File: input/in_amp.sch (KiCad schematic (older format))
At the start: 18 parts, among them J101 Conn_02x02_Odd_Even, U105 LT1028, U106 LT1028, U107 LT1028

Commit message: Changes mostly related to avoiding excess power consumption.  This is mainly by limiting the signal swing to 0..5V and using asymmetric supplies of -4V and +8V.  (Perhaps we can reduce these to 3/7 V.)  Also, I got rid of two stages in the input signal path.
power_budget.xlsx
power.sch
reference_buffer.sch:
Changes related to the new supply voltages, and start on the power supply section.

input_channel.sch
in_amp.sch
antialias_driver.sch:
Reworked the input signal chain to keep a full differential path, rolling the antialias filter
into the ADC driver.  Also, related to change to lower asymmetrical supply voltages, there is
no 20V PP anywhere (the this was for benefit of the antialias filter noise, but that stage is gone).  Also, added zener clamp on VREF in driver.

in_filter.sch: added missing DC bias resistors.
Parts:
- removed C133, C134, C135, C136: 1uF, Capacitor_SMD:C_0603_1608Metric, symbol Device:C_Small
- removed RN103: 1K, Resistor_SMD:R_Array_Convex_4x1206, symbol Device:R_Pack04
- removed U105, U106, U107: LT1028, symbol ilemt_input:opamp_single
- added U101: AD8599, Package_SO:SO-8_5.3x6.2mm_P1.27mm, symbol ilemt_input:OPAMP_DUAL
- R126: value 49.9 -> 100; Notes (none) -> 0.1%
- R127: value 143 -> 243
- R128: value 499 -> 1K; footprint Resistor_SMD:R_1206_3216Metric -> Resistor_SMD:R_0603_1608Metric; Description RES 499 OHM 0.1% 2/5W 1206 -> (none); Digikey 541-3877-1-ND -> (none)
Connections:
- net labels added: +out, -out, V+, V-
- net labels removed: +15V, -15V, out, out_ref
- wire segments 79 -> 47
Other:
- note added: "Both jumpers: gain 16\nJumper 1-2: gain 12\nJumper 3-4: gain 6\nNo jumpers: gain 2\n"
- note added: "C129, C130 give a pole at 30 kHz which is part of the 3rd order\nantialias filter. They also swamp stray capacitance at the\ninverting input due to gain switching network."
- note added: "This is a differential amplifier, like the first part of a 3 opamp style \ninstrumentation amp, but we output to the fully-differential\ndriver/antialias filter in the antialias_driver sheet."
- note removed: "Both jumpers: gain 30\nJumper 1-2: gain 21\nJumper 3-4: gain 10\nNo jumpers: gain 3\nNote that ADC driver has gain 1/2, \nso overall gain is half this\n"
- note removed: "C195, C1230 mainly there to swamp excess capacitance at the \ninverting input due to gain switching network, but also give\nsome band limiting, 144 kHz. The antialias filter gives plenty\nof rejection, so we are not risking compromising CMR by\ntaking a strong cut here (though to first order, mismatch should\nnot matter)."

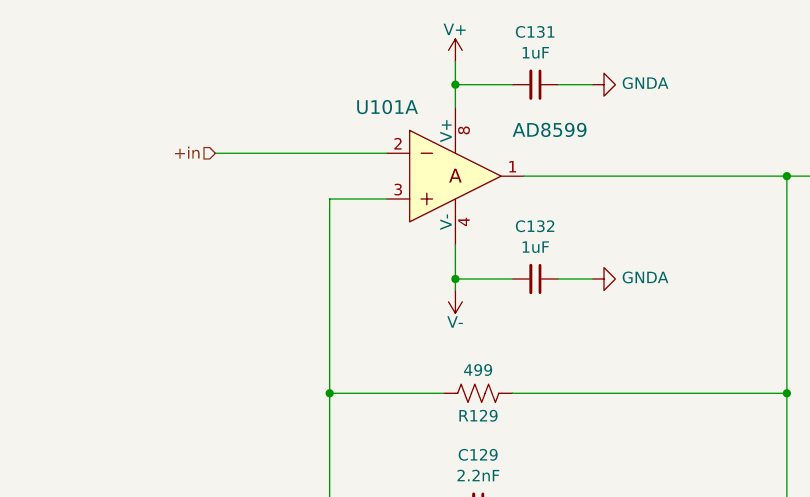
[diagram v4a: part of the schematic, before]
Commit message: Mostly work on power, regulators and distribution.  Also more BOM cleanup.
All of the bypass capacitors are now spec'd and in the DigiKey BOM. TVS zeners are now
spec'd.  Folded together some resistor values and got rid of some 1206 parts that no longer
need that much power rating at the lower supplies.

A affecting all of the input channel sheets is that we now distribute filtered V+, V- and VREF
via sheet ports.  The V+, V- filter is on input_channel.sch and the VREF filter is still in
adc.sch, but is distributed out to the other sheets that need it.

bist_buffer.sch: added buffer for built-in self-test

board_connector.sch: put the input filter for the analog supplies here.

power.sch: added regulators for the supplies.

reference_buffer.sch:
changed components to match those chosen for the V+, V- regulators and added
current steering diodes to bootstrap the reference buffer supply.  This is
necessary because the analog supplies are now derived from VREF.

*.wxsch:
Updates to spice models related to work on supplies.
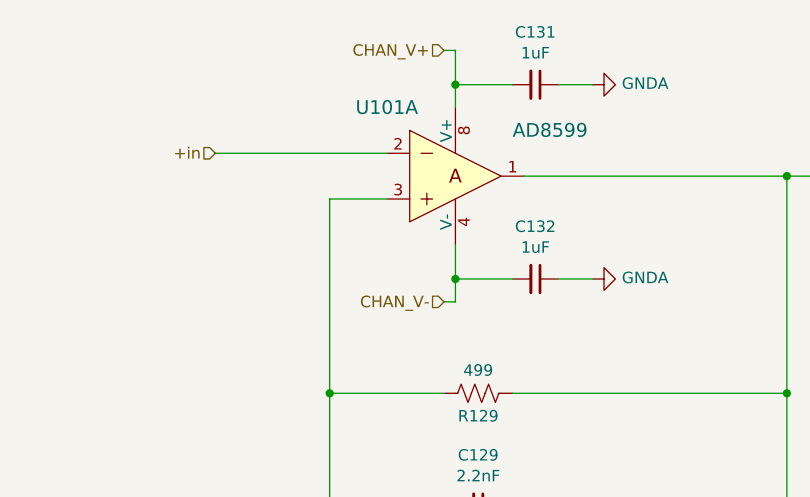
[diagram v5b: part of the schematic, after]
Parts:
- C131, C132: footprint Capacitor_SMD:C_0603_1608Metric -> Capacitor_SMD:C_0805_2012Metric; Description (none) -> CAP CER 1UF 16V X7R 0805; Digikey (none) -> 1276-6471-1-ND; MPN (none) -> CL21B105KOFNNNG
- R128: Notes (none) -> 0.1%
- R129, R130: footprint Resistor_SMD:R_1206_3216Metric -> Resistor_SMD:R_0805_2012Metric; Description RES 499 OHM 0.1% 2/5W 1206 -> RES SMD 499 OHM 0.1% 1/4W 0805; Digikey 541-3877-1-ND -> A110514CT-ND; Notes (none) -> 0.1%
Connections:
- net V+ renamed CHAN_V+
- net V- renamed CHAN_V-
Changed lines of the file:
@@
 EESchema Schematic File Version 4
 LIBS:input_board-cache
-LIBS:input_channel-cache
-LIBS:reference_buffer-cache
 EELAYER 29 0
 EELAYER END
 $Descr A4 11693 8268
 encoding utf-8
-Sheet 6 11
+Sheet 6 12
 Title ""
 Date ""
@@
 Comment4 ""
 $EndDescr
-Wire Wire Line
-	4000 900  4000 1000
 $Comp
 L Device:C_Small C131
@@
 F 0 "C131" V 4121 1000 50  0000 C CNN
 F 1 "1uF" V 4212 1000 50  0000 C CNN
-F 2 "Capacitor_SMD:C_0603_1608Metric" H 4350 1000 50  0001 C CNN
-F 3 "~" H 4350 1000 50  0001 C CNN
+F 2 "Capacitor_SMD:C_0805_2012Metric" H 4350 1000 50  0001 C CNN
+F 3 "https://media.digikey.com/pdf/Data%20Sheets/Samsung%20PDFs/CL_Series_MLCC_ds.pdf" H 4350 1000 50  0001 C CNN
+F 4 "CAP CER 1UF 16V X7R 0805 " H 4350 1000 50  0001 C CNN "Description"
+F 5 "1276-6471-1-ND" H 4350 1000 50  0001 C CNN "Digikey"
+F 6 "CL21B105KOFNNNG" H 4350 1000 50  0001 C CNN "MPN"
 	1    4350 1000
 	0    1    1    0
@@
 F 0 "C132" V 4121 1850 50  0000 C CNN
 F 1 "1uF" V 4212 1850 50  0000 C CNN
-F 2 "Capacitor_SMD:C_0603_1608Metric" H 4350 1850 50  0001 C CNN
-F 3 "~" H 4350 1850 50  0001 C CNN
+F 2 "Capacitor_SMD:C_0805_2012Metric" H 4350 1850 50  0001 C CNN
+F 3 "https://media.digikey.com/pdf/Data%20Sheets/Samsung%20PDFs/CL_Series_MLCC_ds.pdf" H 4350 1850 50  0001 C CNN
+F 4 "CAP CER 1UF 16V X7R 0805 " H 4350 1850 50  0001 C CNN "Description"
+F 5 "1276-6471-1-ND" H 4350 1850 50  0001 C CNN "Digikey"
+F 6 "CL21B105KOFNNNG" H 4350 1850 50  0001 C CNN "MPN"
 	1    4350 1850
 	0    1    1    0
@@
 Wire Wire Line
 	4450 1850 4600 1850
-Wire Wire Line
-	4000 1900 4000 1850
 Connection ~ 4000 1850
 Wire Wire Line
@@
 F 0 "R129" V 4200 2350 50  0000 C CNN
 F 1 "499" V 4000 2350 50  0000 C CNN
-F 2 "Resistor_SMD:R_1206_3216Metric" V 4140 2340 50  0001 C CNN
+F 2 "Resistor_SMD:R_0805_2012Metric" V 4140 2340 50  0001 C CNN
 F 3 "http://www.vishay.com/docs/28758/tnpw_e3.pdf" H 4100 2350 50  0001 C CNN
-F 4 "RES 499 OHM 0.1% 2/5W 1206" H 4100 2350 50  0001 C CNN "Description"
-F 5 "541-3877-1-ND" H 4100 2350 50  0001 C CNN "Digikey"
+F 4 "RES SMD 499 OHM 0.1% 1/4W 0805" H 4100 2350 50  0001 C CNN "Description"
+F 5 "A110514CT-ND" H 4100 2350 50  0001 C CNN "Digikey"
+F 6 "0.1%" H 4100 2350 50  0001 C CNN "Notes"
 	1    4100 2350
 	0    1    1    0
@@
 F 0 "R130" V 4200 5250 50  0000 C CNN
 F 1 "499" V 4000 5250 50  0000 C CNN
-F 2 "Resistor_SMD:R_1206_3216Metric" V 4140 5240 50  0001 C CNN
+F 2 "Resistor_SMD:R_0805_2012Metric" V 4140 5240 50  0001 C CNN
 F 3 "http://www.vishay.com/docs/28758/tnpw_e3.pdf" H 4100 5250 50  0001 C CNN
-F 4 "RES 499 OHM 0.1% 2/5W 1206" H 4100 5250 50  0001 C CNN "Description"
-F 5 "541-3877-1-ND" H 4100 5250 50  0001 C CNN "Digikey"
+F 4 "RES SMD 499 OHM 0.1% 1/4W 0805" H 4100 5250 50  0001 C CNN "Description"
+F 5 "A110514CT-ND" H 4100 5250 50  0001 C CNN "Digikey"
+F 6 "0.1%" H 4100 5250 50  0001 C CNN "Notes"
 	1    4100 5250
 	0    1    1    0
@@
 F 2 "Resistor_SMD:R_0603_1608Metric" V 3940 4040 50  0001 C CNN
 F 3 "http://www.vishay.com/docs/28758/tnpw_e3.pdf" H 3900 4050 50  0001 C CNN
+F 4 "0.1%" H 3900 4050 50  0001 C CNN "Notes"
 	1    3900 4050
 	1    0    0    -1
@@
 This is a differential amplifier, like the first part of a 3 opamp style \ninstrumentation amp, but we output to the fully-differential\ndriver/antialias filter in the antialias_driver sheet.
 $Comp
-L ilemt_input:V+ #PWR0132
-U 1 1 5E4F57E2
-P 4000 900
-F 0 "#PWR0132" H 4000 750 50  0001 C CNN
-F 1 "V+" H 4000 1040 50  0000 C CNN
-F 2 "" H 4000 900 50  0001 C CNN
-F 3 "" H 4000 900 50  0001 C CNN
-	1    4000 900
-	1    0    0    -1
-$EndComp
-$Comp
-L ilemt_input:V- #PWR0139
-U 1 1 5E4F5C06
-P 4000 2000
-F 0 "#PWR0139" H 4000 1850 50  0001 C CNN
-F 1 "V-" H 4000 1960 50  0000 C CNN
-F 2 "" H 4000 2100 50  0001 C CNN
-F 3 "" H 4000 2100 50  0001 C CNN
-	1    4000 2000
-	1    0    0    -1
-$EndComp
-$Comp
 L ilemt_input:OPAMP_DUAL U101
 U 1 1 5E501ACE
@@
 	5450 5250 5450 6050
 Connection ~ 5450 5250
+Text HLabel 3950 850  0    50   Input ~ 0
+CHAN_V+
+Text HLabel 3950 1950 0    50   Input ~ 0
+CHAN_V-
+Wire Wire Line
+	3950 850  4000 850
+Wire Wire Line
+	4000 850  4000 1000
+Wire Wire Line
+	3950 1950 4000 1950
+Wire Wire Line
+	4000 1850 4000 1950
 $EndSCHEMATC

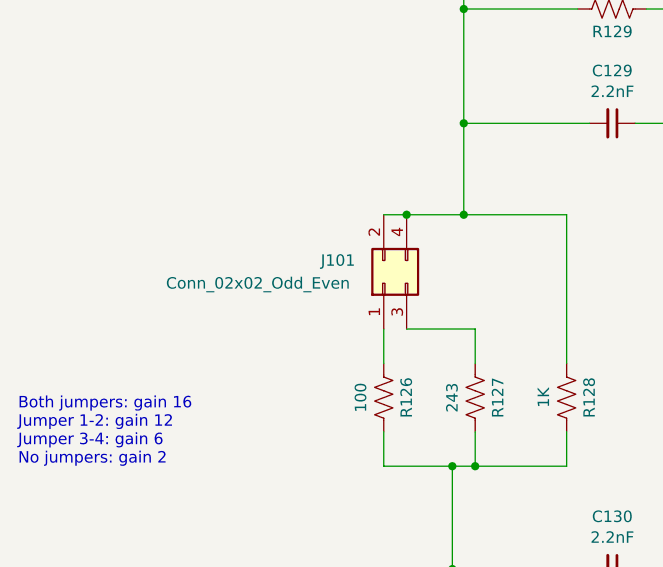
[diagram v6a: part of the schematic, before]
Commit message: Cleanup to get ready to start board layout. I had to get rid off all the bus signals, since in Kicad busses don't work that way.  Added a couple testpoints; many more needed.
Work on component placement in PCB.  I changed DGND to plain GND and "protective earth" to
"earth" (for chassis ground).  Chassis ground is now connected on the board only via a capacitor.
I had to fix the connector footprint to match the pin numbers on the symbol (there was a case
difference).
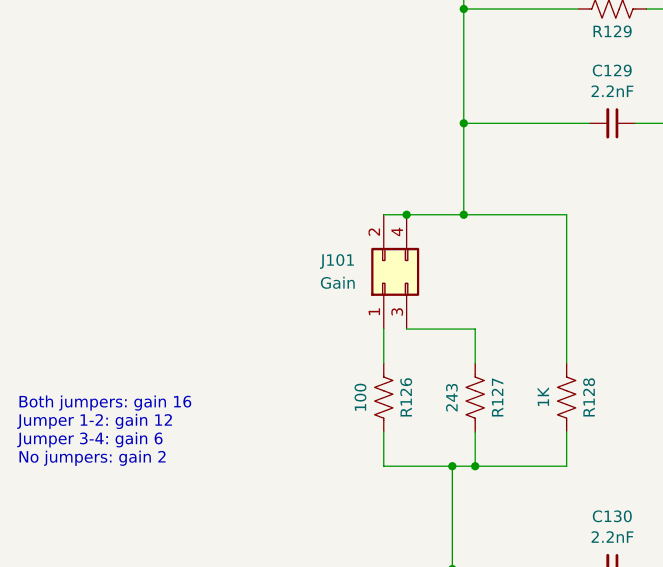
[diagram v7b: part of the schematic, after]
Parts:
- J101: value Conn_02x02_Odd_Even -> Gain; footprint (none) -> Connector_PinHeader_2.00mm:PinHeader_2x02_P2.00mm_Vertical_SMD; Description (none) -> CONN HEADER SMD 4POS 2MM; Digikey (none) -> S6009-02-ND
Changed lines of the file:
@@
 AR Path="/5DFCF14D/5E195558/5DE6EE15" Ref="J101"  Part="1"
 F 0 "J101" V 3200 3750 50  0000 C CNN
-F 1 "Conn_02x02_Odd_Even" V 3100 4100 50  0000 C CNN
-F 2 "" H 3100 3550 50  0001 C CNN
+F 1 "Gain" V 3100 3750 50  0000 C CNN
+F 2 "Connector_PinHeader_2.00mm:PinHeader_2x02_P2.00mm_Vertical_SMD" H 3100 3550 50  0001 C CNN
 F 3 "~" H 3100 3550 50  0001 C CNN
+F 4 "CONN HEADER SMD 4POS 2MM" H 3100 3550 50  0001 C CNN "Description"
+F 5 "S6009-02-ND" H 3100 3550 50  0001 C CNN "Digikey"
 	1    3100 3550
 	0    -1   -1   0

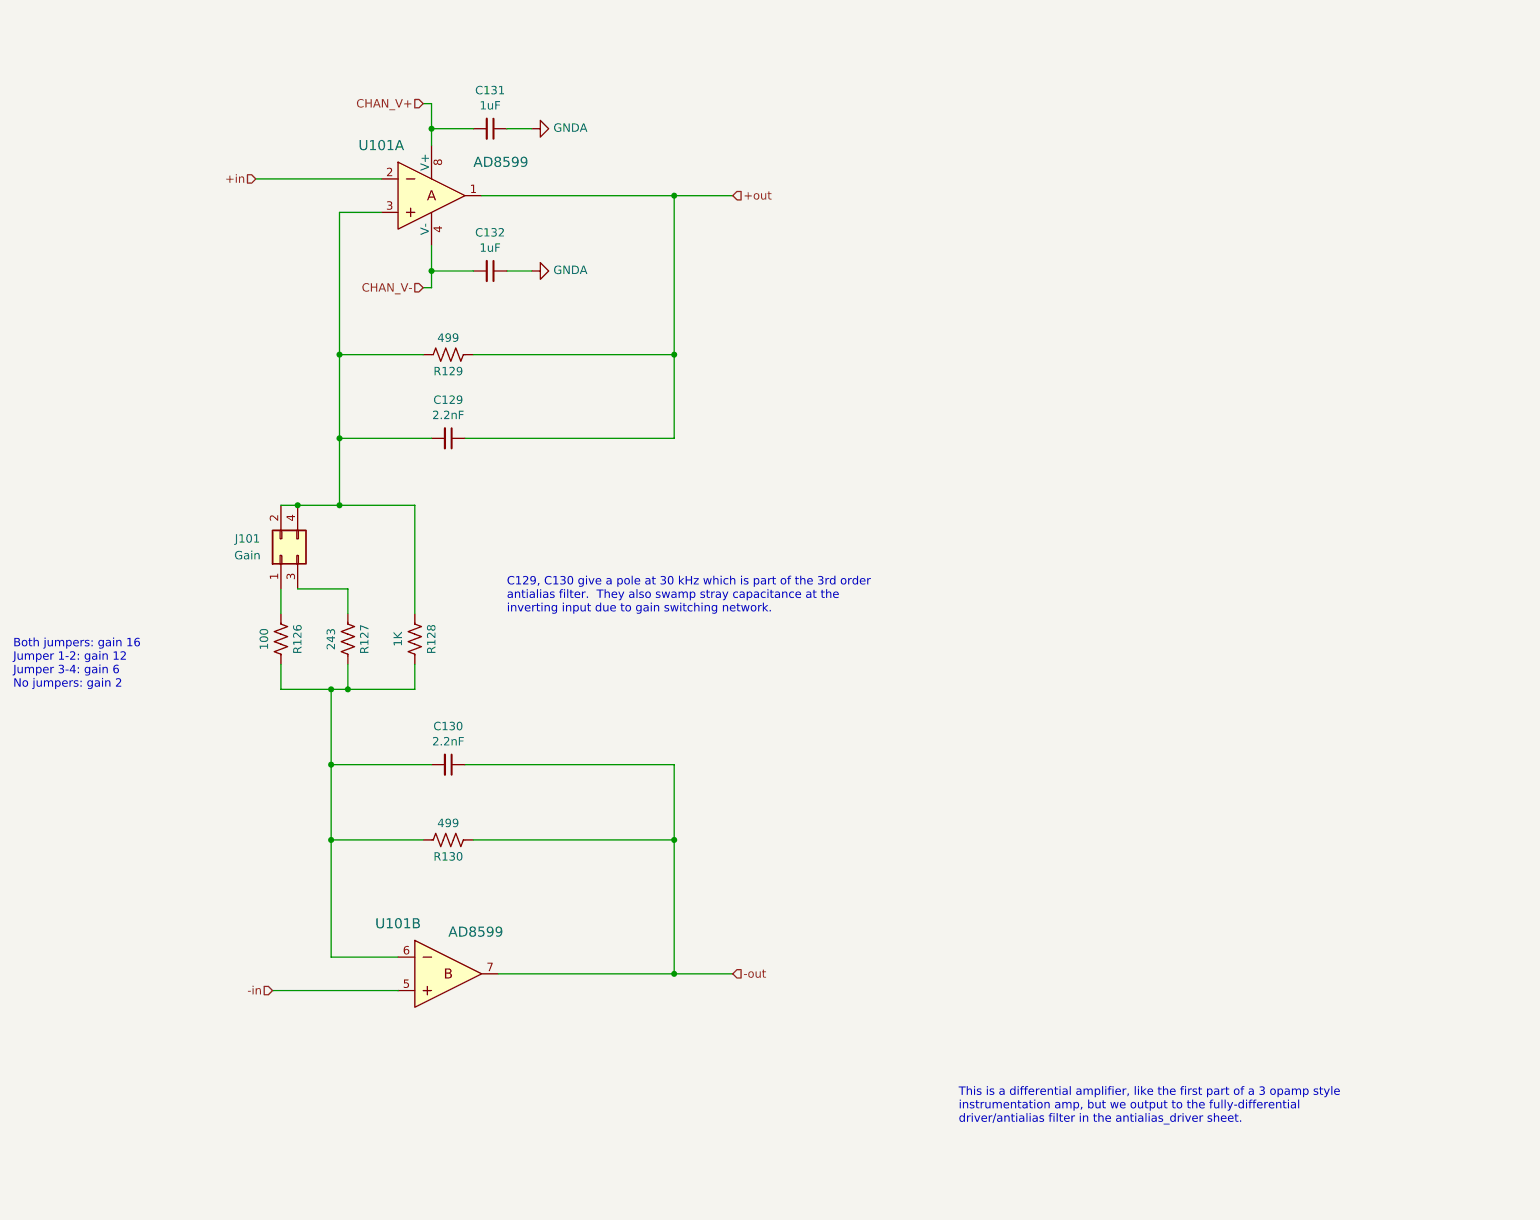
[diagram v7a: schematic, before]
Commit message: Changed board connector to PCIe 8x, added test points, cleanup of component values. Add LVDS Rx termination, bypass caps.
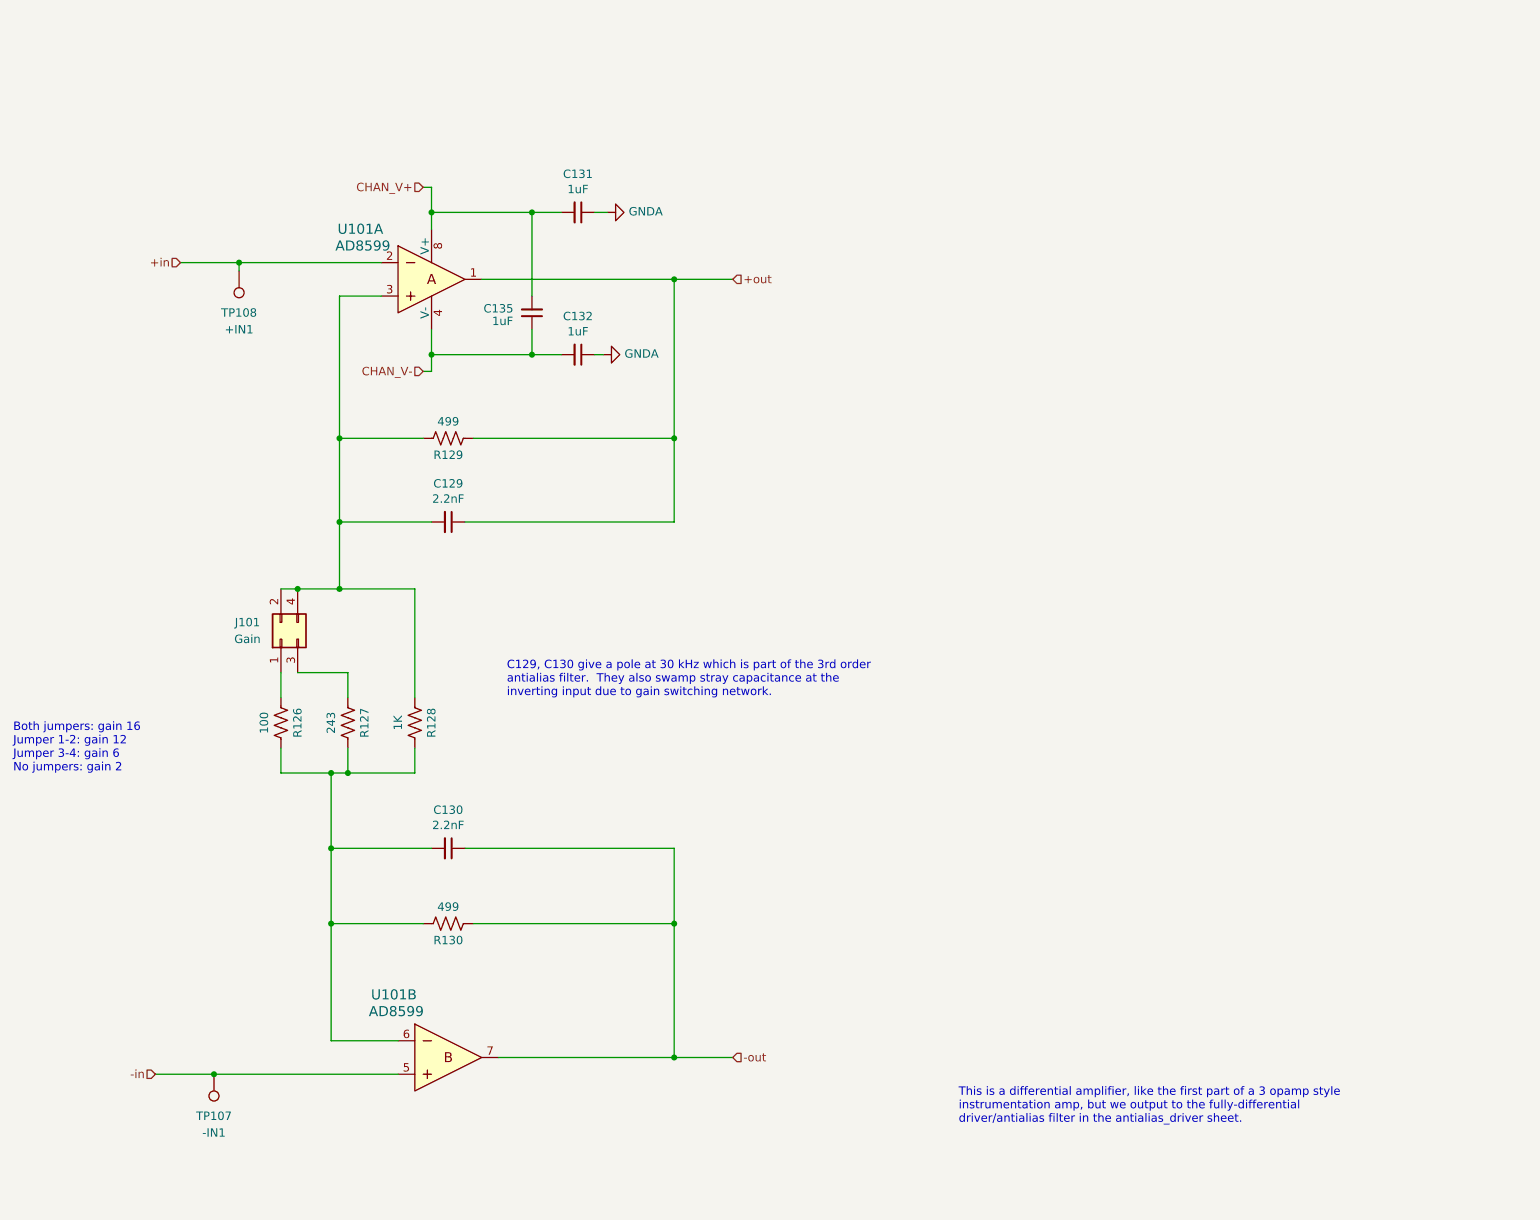
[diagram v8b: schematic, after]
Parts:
- added C135: 1uF, Capacitor_SMD:C_0805_2012Metric, symbol Device:C_Small
- added TP107: -IN1, TestPoint:TestPoint_THTPad_D1.5mm_Drill0.7mm, symbol Connector:TestPoint
- added TP108: +IN1, TestPoint:TestPoint_THTPad_D1.5mm_Drill0.7mm, symbol Connector:TestPoint
- C129, C130: Notes 1% C0G -> 2% C0G
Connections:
- net +in: now also TP108.1
- net -in: now also TP107.1
- net CHAN_V+: now also C135.2
- net CHAN_V-: now also C135.1
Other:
- moved on the sheet: C129, C130, C131, C132, J101, R126, R127, R128, R129, R130, U101A, U101B
